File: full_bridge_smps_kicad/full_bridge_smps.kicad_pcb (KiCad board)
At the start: 2 copper layers, 101.6 x 104.1 mm, 1 part, among them U1 UCC28950PW

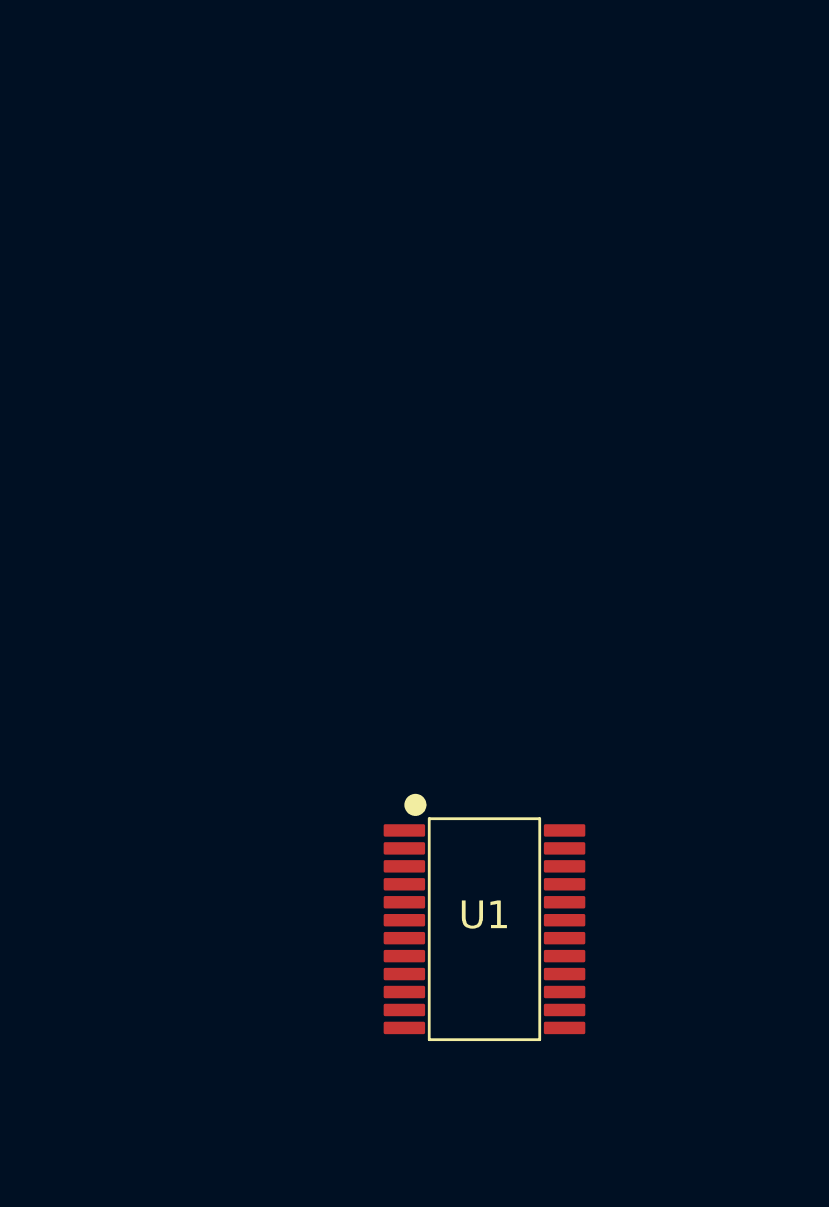
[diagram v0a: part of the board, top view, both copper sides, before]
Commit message: Adding schematic page for interleaved CCM PFC
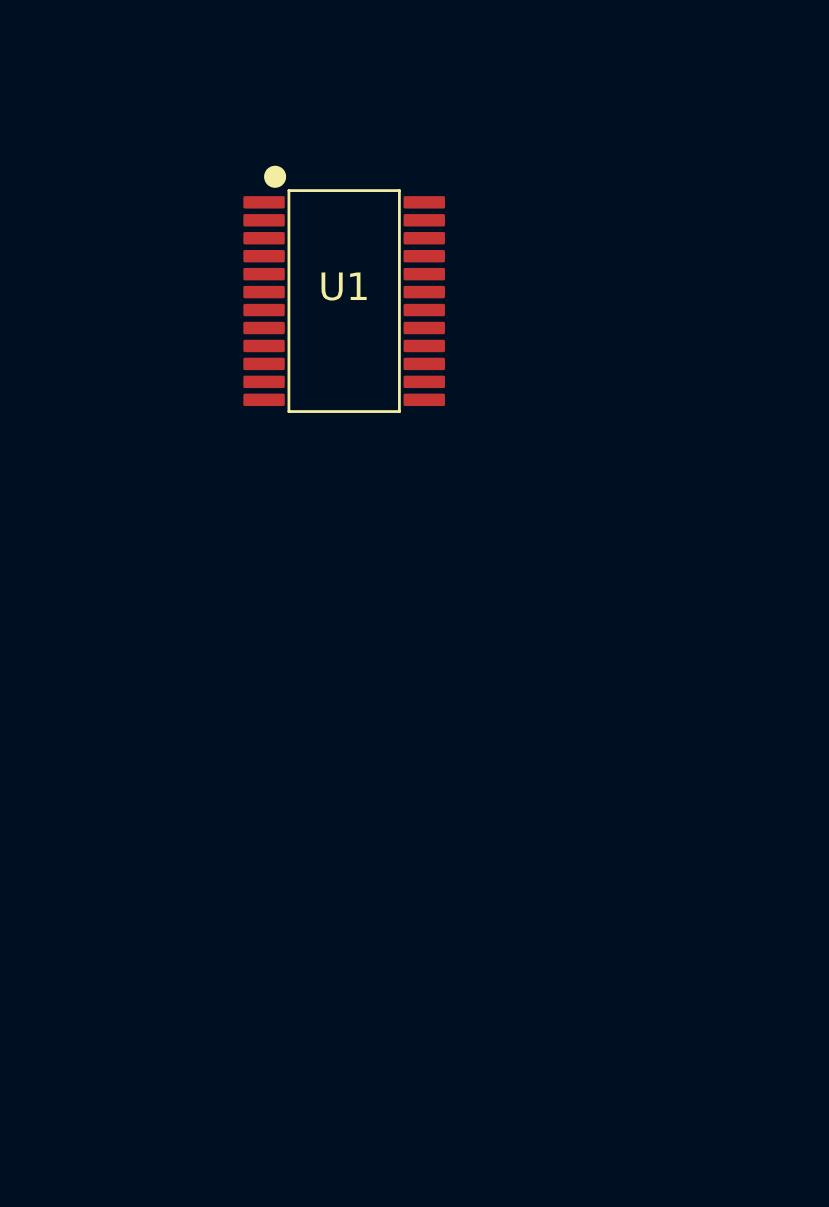
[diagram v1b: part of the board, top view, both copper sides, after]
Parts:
- moved U1 23.3 mm to (106.3, 70.2)
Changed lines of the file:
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@@
   (net 24 "unconnected-(U1-GND-Pad24)")
   (footprint "full bridge smps:UCC28950" (layer "F.Cu")
-    (at 111.4 92.945)
+    (at 106.32 70.205)
     (property "Sheetfile" "full_bridge_smps.kicad_sch")
     (property "Sheetname" "")
